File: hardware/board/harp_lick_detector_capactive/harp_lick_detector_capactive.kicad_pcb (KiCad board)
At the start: 4 copper layers, 80 x 50 mm, 123 parts, among them J1 Conn_01x03_Male, J2 Conn_01x03_Male, J3 Conn_Triaxial, J4 AudioJack3, J5 USB_C_Receptacle_USB2.0, J6 Barrel_Jack_Switch, J7 Conn_Coaxial, SW1 SW_Push, U1 ADS7029, U10 CD74AC04, U11 LM27762, U12 LT3030, U2 TPD2EUSB30, U3 ADUM4160, U4 RP2040, U5 W25Q128JVS, U6 LTC6263, U7 LTC6268xS8-10, U8 REF3433QDBVRQ1, U9 AD9833xRM, X1 ECS-TXO-2016

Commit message: draft consolidated board
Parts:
- removed C38: 160pF, Capacitor_SMD:C_0402_1005Metric_Pad0.74x0.62mm_HandSolder
- removed J1: Conn_01x03_Male, Connector_PinHeader_2.54mm:PinHeader_1x03_P2.54mm_Vertical
- removed the REF** at (107.9, 71.1)
- removed the REF** at (107.9, 115.1)
- removed the REF** at (181.9, 115.1)
- removed the REF** at (181.9, 71.1)
- removed U1: ADS7029, Package_SO:VSSOP-8_2.3x2mm_P0.5mm
- added C32: 10nF, Capacitor_SMD:C_0402_1005Metric, F.Cu at (132.0, 88.6)
- added C52: 300pF, Capacitor_SMD:C_0402_1005Metric, F.Cu at (141.8, 99.0)
- added G1: LOGO, LOGO, B.Cu at (119.3, 79.7)
- added G3: LOGO, LOGO, B.Cu at (179.8, 106.7)
- added H1: MountingHole_Pad, kicad_component_library:Terminal_Keystone_779x_EdgeMount_Horizontal, F.Cu at (112.5, 106.0)
- added R42: 16, Resistor_SMD:R_0402_1005Metric, F.Cu at (140.3, 98.5)
- added R43: 16, Resistor_SMD:R_0402_1005Metric, F.Cu at (140.3, 99.5)
- added R44: 49.9, Resistor_SMD:R_0402_1005Metric, F.Cu at (147.5, 97.6)
- added REF**: MountingHole_3.2mm_M3_DIN965, MountingHole:MountingHole_3.2mm_M3_DIN965, F.Cu at (181.9, 115.0)
- added REF**: MountingHole_3.2mm_M3_DIN965, MountingHole:MountingHole_3.2mm_M3_DIN965, F.Cu at (181.9, 71.0)
- added REF**: MountingHole_3.2mm_M3_DIN965, MountingHole:MountingHole_3.2mm_M3_DIN965, F.Cu at (107.9, 71.0)
- added REF**: MountingHole_3.2mm_M3_DIN965, MountingHole:MountingHole_3.2mm_M3_DIN965, F.Cu at (107.9, 115.0)
- added REF1: OSHW-Logo2_7.3x6mm_SilkScreen, Symbol:OSHW-Logo2_7.3x6mm_SilkScreen, B.Cu at (113.7, 114.8)
- added U13: ADS7049, Package_SO:VSSOP-8_2.3x2mm_P0.5mm, F.Cu at (144.7, 99.9)
- C37: value 160pF -> 100nF
- C43, C44, C50, C51: footprint Capacitor_SMD:C_0603_1608Metric -> Capacitor_SMD:C_0402_1005Metric
- J7: footprint Connector_Coaxial:SMA_Samtec_SMA-J-P-X-ST-EM1_EdgeMount -> kicad_component_library:SMA_TE_Connectivity_CONSMA002-SMD-G-T_Horizontal
- R17: footprint Resistor_SMD:R_0805_2012Metric -> Resistor_SMD:R_0402_1005Metric_Pad0.72x0.64mm_HandSolder
- R25: value 100K -> 10K
- R26: value 3K2 -> 320
- R27: value 49K9 -> 100K
- R28: value 1K02 -> 49.9; footprint Resistor_SMD:R_0402_1005Metric_Pad0.72x0.64mm_HandSolder -> Resistor_SMD:R_0402_1005Metric
- R29: value 100K -> 49.9; footprint Resistor_SMD:R_0402_1005Metric_Pad0.72x0.64mm_HandSolder -> Resistor_SMD:R_0402_1005Metric
- R32, R33, R34, R35: footprint Resistor_SMD:R_0603_1608Metric_Pad0.98x0.95mm_HandSolder -> Resistor_SMD:R_0402_1005Metric
- moved C11 74.8 mm to (144.6, 104.1), turned to 180 degrees
- moved C27 74.7 mm to (141.1, 115.4)
- moved C7 70.4 mm to (157.8, 89.9), turned to 180 degrees
- moved C26 65.1 mm to (141.1, 114.1)
- moved C6 64.2 mm to (144.4, 94.4)
- moved C24 61.9 mm to (129.0, 91.1), turned to -90 degrees
- moved C33 59.9 mm to (141.9, 86.1), turned to -90 degrees
- moved C18 58.6 mm to (157.8, 90.9), turned to 180 degrees
- moved R30 53.6 mm to (174.7, 77.6)
- moved C4 53.3 mm to (141.7, 90.6), turned to 90 degrees
- moved C25 52.7 mm to (136.4, 91.8), turned to 90 degrees
- moved R31 52.1 mm to (174.7, 79.2)
- moved R20 49.9 mm to (132.4, 96.4), turned to 90 degrees
- moved R28 49.2 mm to (148.5, 97.6), turned to 90 degrees
- moved R29 45.8 mm to (149.5, 97.6), turned to 90 degrees
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- renumbered G*** to G2
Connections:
- net /100KHz Sine Wave/xtal_out renamed /100KHz Sine Wave/xtal_in
- C31 pad 2: Net-(U6D--) -> Net-(U6B--)
- C37 pad 1: Net-(C37-Pad1) -> GND1
- C37 pad 2: /100KHz Sine Wave/VSINE -> VBUS
- C43 pad 1: +2V5 -> GND
- C43 pad 2: GND -> +2V5
- C44 pad 1: -2V5 -> GND
- C44 pad 2: GND -> -2V5
- J5 pad S1: unconnected-(J5-SHIELD-PadS1) -> GND1
- R17 pad 1: Net-(U7--) -> GND
- R17 pad 2: GND -> Net-(U7--)
- R20 pad 1: Net-(U6D--) -> Net-(U6B--)
- R21 pad 2: Net-(U6A--) -> Net-(U6D--)
- R22 pad 1: Net-(U6A--) -> Net-(U6D--)
- R23 pad 1: Net-(U1-AINP) -> Net-(U6C-+)
- R24 pad 2: Net-(U1-AINP) -> Net-(U6C-+)
- R25 pad 1: Net-(U6B-+) -> Net-(C32-Pad1)
- R26 pad 1: Net-(U6B-+) -> Net-(C32-Pad1)
- R27 pad 1: Net-(U6B--) -> GND
- R27 pad 2: Net-(C37-Pad1) -> Net-(U6A-+)
- R28 pad 1: GND -> Net-(U13-SDO)
- R28 pad 2: Net-(C37-Pad1) -> /Harp Core RP2040 + Isolated USB/PIO_POCI
- R29 pad 1: Net-(U6C--) -> Net-(U13-SCLK)
- R29 pad 2: /100KHz Sine Wave/VSINE -> /Harp Core RP2040 + Isolated USB/PIO_SCK
- U4 pad 29: unconnected-(U4-GPIO18-Pad29) -> /Harp Core RP2040 + Isolated USB/PIO_CS
- U4 pad 30: unconnected-(U4-GPIO19-Pad30) -> /Harp Core RP2040 + Isolated USB/PIO_POCI
- U4 pad 31: unconnected-(U4-GPIO20-Pad31) -> /Harp Core RP2040 + Isolated USB/PIO_SCK
- U6 pad 1: Net-(R22-Pad2) -> /100KHz Sine Wave/VSINE
- U6 pad 10: /100KHz Sine Wave/VSINE -> Net-(U6C--)
- U6 pad 12: GND -> Net-(U6C-+)
- U6 pad 16: Net-(C30-Pad2) -> Net-(R22-Pad2)
- U6 pad 2: Net-(U6A--) -> /100KHz Sine Wave/VSINE
- U6 pad 3: GND -> Net-(U6A-+)
- U6 pad 5: Net-(U6B-+) -> GND
- U6 pad 7: Net-(U6B--) -> Net-(C30-Pad2)
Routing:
- net GND: track 9.71 -> 104.9 mm, vias 6 -> 55
- net +3V3: track 0.00 -> 87.9 mm, vias 0 -> 23
- net /Harp Core RP2040 + Isolated USB/TTL_OUT: track 0.00 -> 38.7 mm
- net GND1: track 0.00 -> 38.6 mm, vias 0 -> 2
- net Net-(U4-GPIO25): track 0.00 -> 36.4 mm, vias 0 -> 2
- net +5V: track 0.00 -> 32.0 mm, vias 0 -> 9
- net Net-(U4-GPIO24): track 0.00 -> 29.1 mm, vias 0 -> 2
- net /Harp Core RP2040 + Isolated USB/QSPI_CS: track 0.00 -> 28.4 mm
- net VREF_3V3: track 0.00 -> 24.5 mm
- net /Lick Detection Analog Front End/triax_inner_shield: track 30.1 -> 54.3 mm, vias 0 -> 20
- net /Harp Core RP2040 + Isolated USB/HARP_CLK_SYNC: track 0.00 -> 23.2 mm, vias 0 -> 1
- net +1V1: track 0.00 -> 21.5 mm
- net VBUS: track 0.00 -> 20.5 mm
- net Net-(U9-VOUT): track 0.00 -> 18.5 mm
- net /Harp Core RP2040 + Isolated USB/QSPI_D1: track 0.00 -> 18.4 mm
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- added copper zone on In2.Cu, net +2V5
- added copper zone on In2.Cu, net +3V3
- added copper zone on In2.Cu, net +5V
- added copper zone on In2.Cu, net -2V5
- added copper zone on F.Cu, net GND1
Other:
- board text added: "6-20VDC"
- board text added: "Bootsel"
- board text added: "Chassis Ground"
- board text added: "GND"
- board text added: "Harp Sync Input ↑"
- board text added: "Isolated USB"
- board text added: "Lick Tube Input ↑"
- board text added: "Lickety Split Lick Detector"
- board text added: "RX"
- board text added: "Rodent lick detection sensing made lickety-split."
- board text added: "Setup Notes: • The ground lug must be connected to the chassis ground of the rig. • USB and 3.5mm (Harp) connections are not needed if solely using the TTL output."
- board text added: "Source Files & Setup ↓"
- board text added: "TTL Lick Detection Signal ↘"
- board text added: "TX"
- board text added: "v0.5.0, Aug 31, 2023"
- board text removed: "Ephys-Compatible Lick Detector, Rev 1"
- board text removed: "FIXME: add ground terminal Lug."
- board text removed: "FIXME: add more test points. * Signals * Power Supplies"
- board text removed: "FIXME: change SMA connector to right angle SMD. (Needs more vertical space from headphone jack.)"
- board text removed: "Setup Notes: * The ground lug must be connected to the chassis ground of the rig. * The USB port is magnetically coupled but not electrically connected to the PC. * USB and 3.5mm (Harp) connections are not needed if solely using the TTL output."
- board text removed: "https://github.com/AllenNeuralDynamics/harp.device.lick-detector"

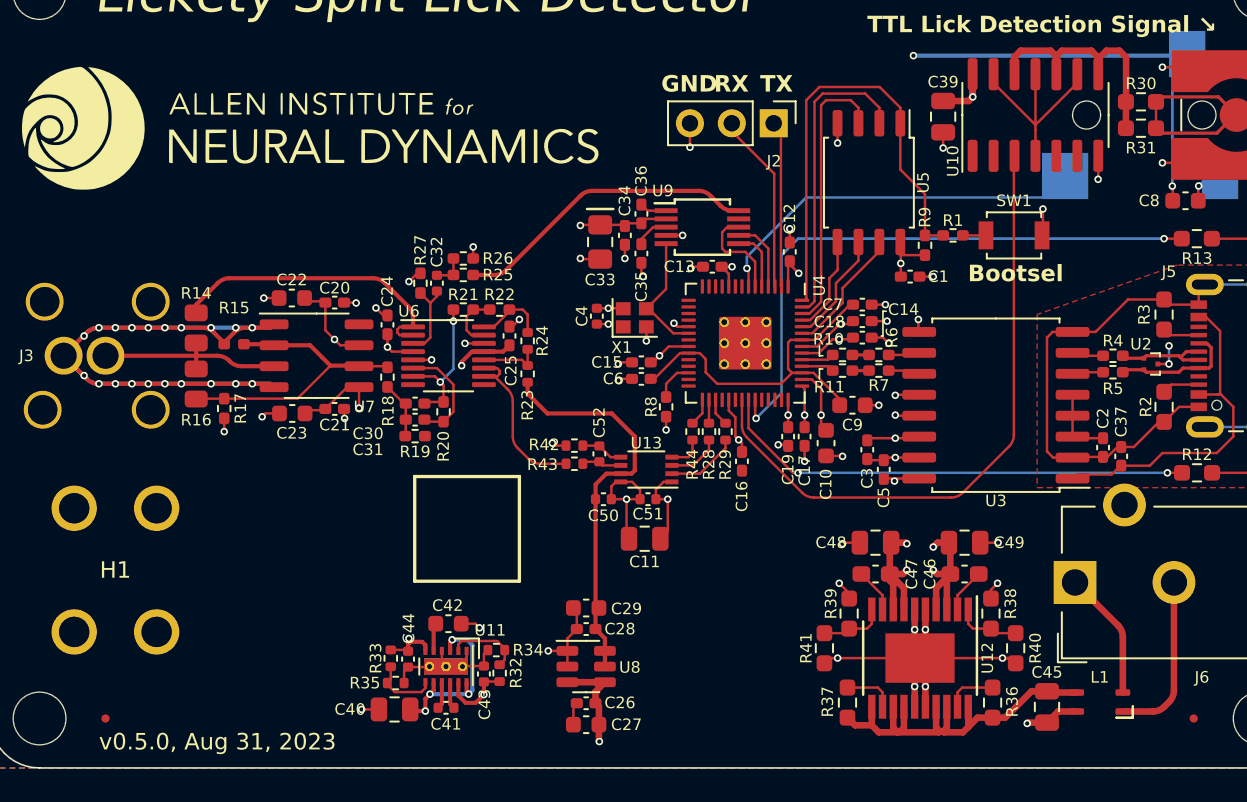
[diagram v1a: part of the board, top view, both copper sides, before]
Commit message: remove hand-soldering footprints
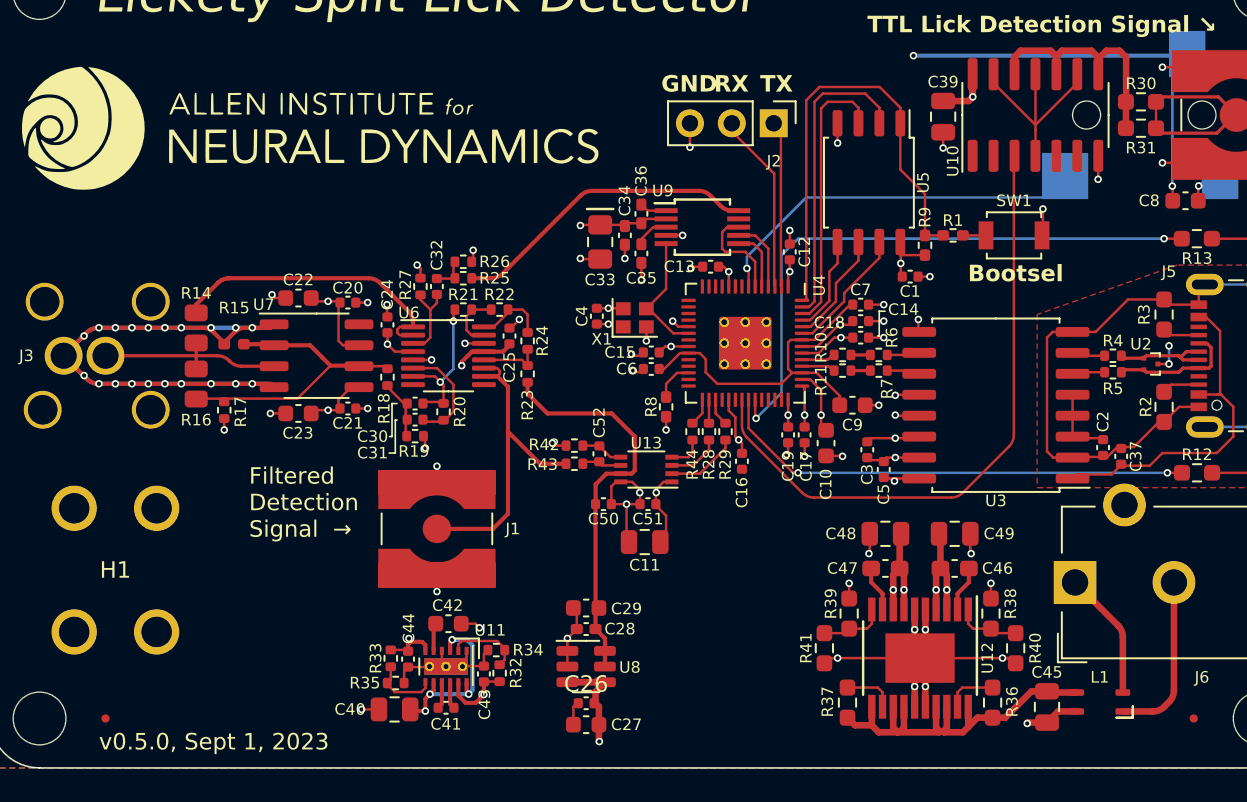
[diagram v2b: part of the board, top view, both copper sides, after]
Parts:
- added J1: Conn_Coaxial, Connector_Coaxial:SMA_Amphenol_132134-10_Vertical, F.Cu at (132.0, 103.5)
- C1, C12, C13, C14, C15, C16, C17, C18, C19, C2, C20, C21, C24, C25, C26, C3, C30, C31, C37, C5, C6, C7: footprint Capacitor_SMD:C_0402_1005Metric_Pad0.74x0.62mm_HandSolder -> Capacitor_SMD:C_0402_1005Metric
- R10, R11, R17, R18, R19, R20, R21, R22, R25, R26, R27, R4, R5, R6, R7: footprint Resistor_SMD:R_0402_1005Metric_Pad0.72x0.64mm_HandSolder -> Resistor_SMD:R_0402_1005Metric
- moved C15 0.85 mm to (145.0, 92.8)
- moved C6 0.85 mm to (145.0, 93.8)
- moved C48 0.81 mm to (159.2, 103.8)
- moved C49 0.81 mm to (163.4, 103.8)
- moved C21 0.80 mm to (126.6, 96.2)
- moved C20 0.80 mm to (126.6, 89.8)
- moved C46 0.69 mm to (163.4, 105.9)
- moved C47 0.69 mm to (159.2, 105.9)
- moved C22 0.40 mm to (123.6, 89.5)
- moved C23 0.38 mm to (123.6, 96.5)
- moved C50 0.30 mm to (142.1, 102.0)
- moved C51 0.30 mm to (144.8, 102.0)
- moved C11 0.20 mm to (144.6, 104.3)
- moved C32 0.20 mm to (132.0, 88.8)
- moved R25 0.20 mm to (133.6, 88.3)
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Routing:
- net Net-(J1-In): track 11.0 -> 20.8 mm
- net +3V3: track 87.9 -> 84.7 mm
- net -2V5: track 12.2 -> 10.8 mm
- net +5V: track 32.0 -> 30.8 mm
- net GND: track 104.9 -> 105.1 mm, vias 55 -> 59
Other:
- board text added: "Filtered Detection Signal →"
- board text added: "v0.5.0, Sept 1, 2023"
- board text removed: "v0.5.0, Aug 31, 2023"

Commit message: update footprints; populate bom
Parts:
- C28, C34, C35, C36: footprint Capacitor_SMD:C_0402_1005Metric_Pad0.74x0.62mm_HandSolder -> Capacitor_SMD:C_0402_1005Metric
- C46, C47: footprint Capacitor_SMD:C_0603_1608Metric_Pad1.08x0.95mm_HandSolder -> Capacitor_SMD:C_0402_1005Metric
- R1, R8, R9: footprint Resistor_SMD:R_0402_1005Metric_Pad0.72x0.64mm_HandSolder -> Resistor_SMD:R_0402_1005Metric
- R12, R13, R38, R39, R40, R41: footprint Resistor_SMD:R_0603_1608Metric_Pad0.98x0.95mm_HandSolder -> Resistor_SMD:R_0402_1005Metric
- R26: value 320 -> 330
- moved R13 1.81 mm to (179.9, 85.9)
- moved R12 1.80 mm to (179.9, 100.1)
- moved R40 1.61 mm to (165.5, 110.9), turned to 90 degrees
- moved R41 1.61 mm to (157.1, 110.9), turned to 90 degrees
- moved R8 0.50 mm to (145.9, 95.6)
- moved C46 0.45 mm to (163.0, 105.7), turned to 0 degrees
- moved C47 0.45 mm to (159.6, 105.7), turned to 180 degrees
- moved C48 0.41 mm to (159.1, 104.2)
- moved C49 0.41 mm to (163.5, 104.2)
- moved R38 0.38 mm to (165.5, 109.0)
- moved R39 0.38 mm to (157.1, 109.0)
- moved C35 0.30 mm to (144.4, 86.5)
- moved C45 0.30 mm to (169.0, 114.0)
- moved C34 0.20 mm to (143.4, 85.5)
- moved X1 0.20 mm to (144.0, 90.5)
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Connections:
- C46 pad 1: Net-(U12-BYP1) -> +5V
- C46 pad 2: +5V -> Net-(U12-BYP1)
- C47 pad 1: Net-(U12-BYP2) -> +3V3
- C47 pad 2: +3V3 -> Net-(U12-BYP2)
- R40 pad 1: Net-(U12-ADJ1) -> GND
- R40 pad 2: GND -> Net-(U12-ADJ1)
- R41 pad 1: Net-(U12-ADJ2) -> GND
- R41 pad 2: GND -> Net-(U12-ADJ2)
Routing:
- net GND: track 105.1 -> 95.4 mm
- net Net-(U4-GPIO25): track 36.4 -> 38.6 mm
- net Net-(U4-GPIO24): track 29.1 -> 31.3 mm
- net +3V3: track 84.7 -> 82.5 mm
- net +5V: track 30.8 -> 29.3 mm
- net Net-(D2-A): track 2.93 -> 1.52 mm
- net Net-(D1-A): track 2.91 -> 1.52 mm
- net Net-(U12-ADJ2): track 3.98 -> 3.11 mm
- net Net-(U12-ADJ1): track 3.98 -> 3.11 mm

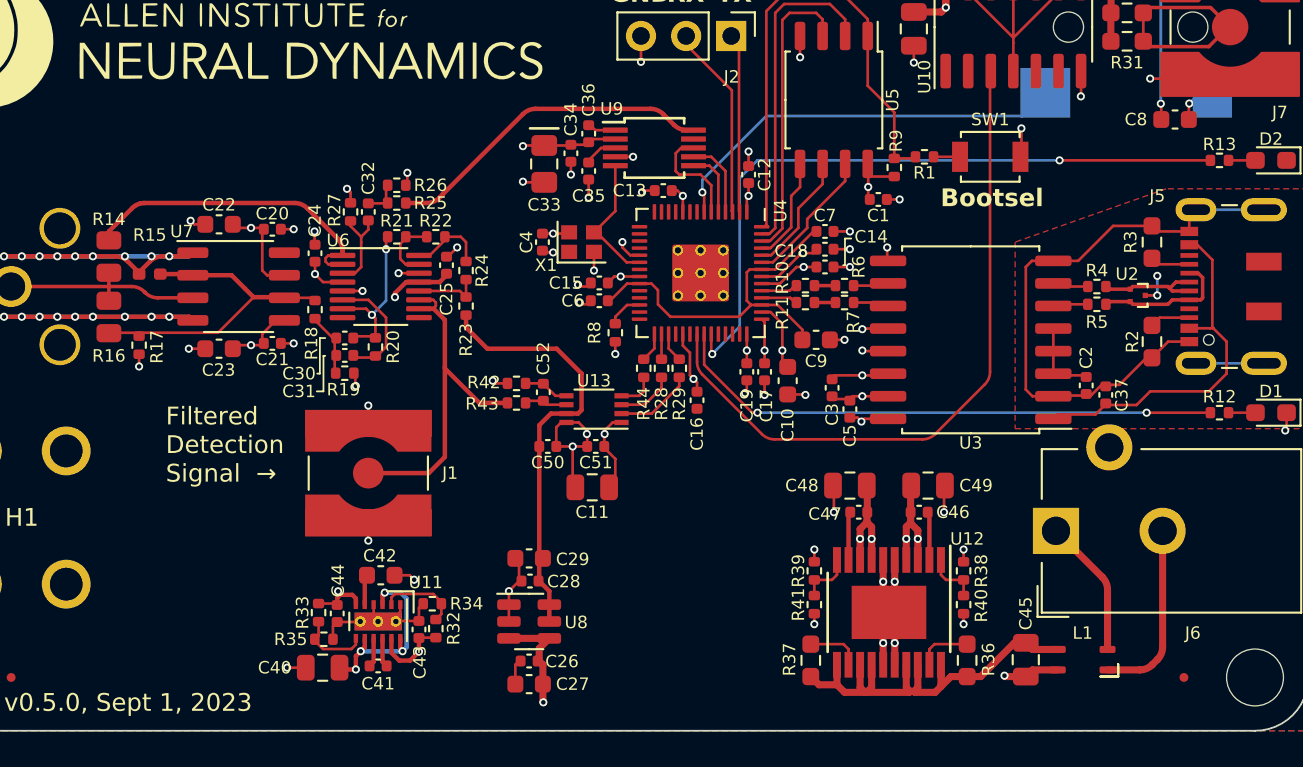
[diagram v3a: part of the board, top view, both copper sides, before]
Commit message: consolidate components; add extra decoupling cap to voltage divider
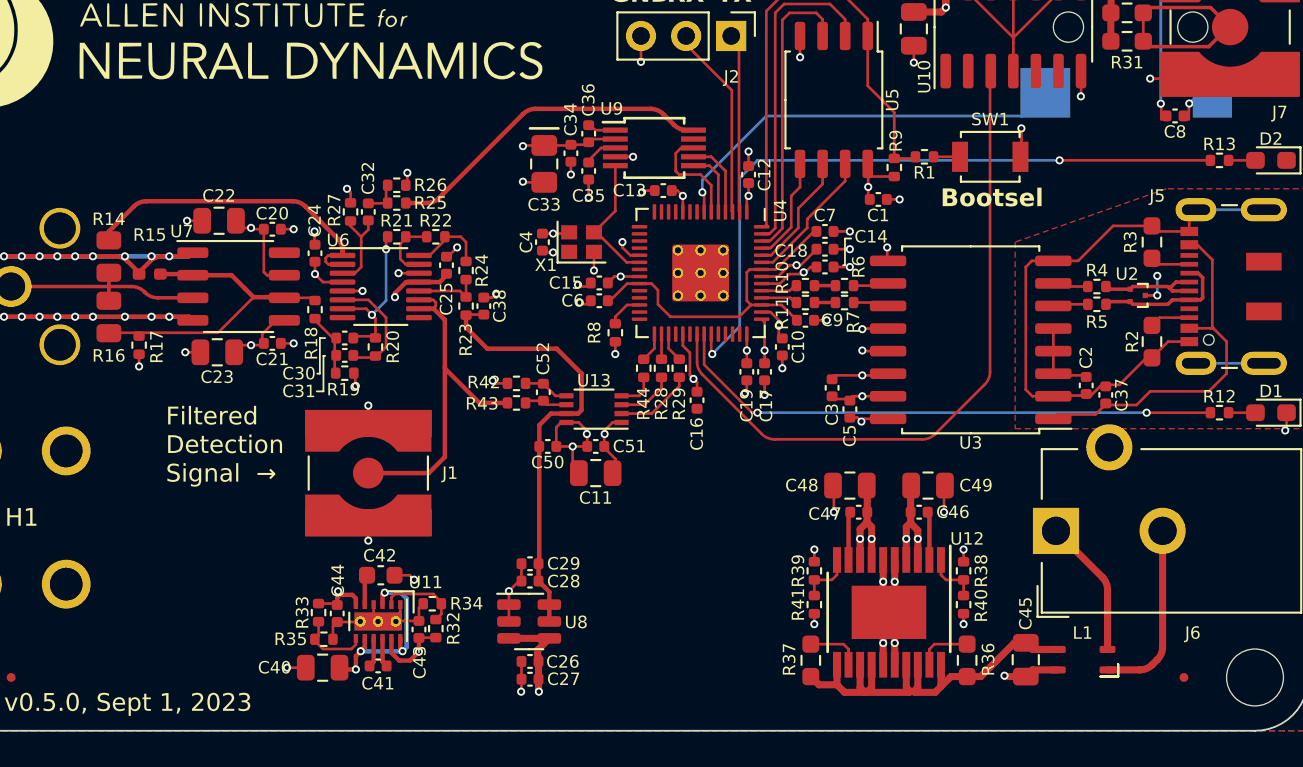
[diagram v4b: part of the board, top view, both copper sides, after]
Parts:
- added C38: 100nF, Capacitor_SMD:C_0402_1005Metric, F.Cu at (138.5, 94.1)
- C10, C8, C9: footprint Capacitor_SMD:C_0603_1608Metric -> Capacitor_SMD:C_0402_1005Metric
- C22, C23: footprint Capacitor_SMD:C_0603_1608Metric -> Capacitor_SMD:C_0805_2012Metric
- C27, C29: value 10uF -> 1uF; footprint Capacitor_SMD:C_0603_1608Metric -> Capacitor_SMD:C_0402_1005Metric
- moved C10 1.92 mm to (155.3, 96.4)
- moved C9 1.25 mm to (156.6, 94.9)
- moved C11 0.82 mm to (144.8, 103.5)
- moved C29 0.30 mm to (141.1, 108.6), turned to 180 degrees
- moved C27 0.28 mm to (141.1, 115.1), turned to 180 degrees
- moved C23 0.22 mm to (123.5, 96.7)
- moved C22 0.20 mm to (123.6, 89.3)
- moved C8 0.20 mm to (177.4, 83.4)
- moved C26 0.06 mm to (141.1, 114.1)
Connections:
- C27 pad 1: GND -> +5V
- C27 pad 2: +5V -> GND
- C29 pad 1: GND -> VREF_3V3
- C29 pad 2: VREF_3V3 -> GND
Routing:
- net +3V3: track 82.5 -> 79.9 mm
- net +1V1: track 20.8 -> 19.7 mm
- net VREF_3V3: track 24.2 -> 25.1 mm
- net +5V: track 29.3 -> 28.7 mm
- net GND: track 95.4 -> 94.9 mm, vias 59 -> 61
